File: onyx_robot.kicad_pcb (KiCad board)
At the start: 2 copper layers, 50 x 50 mm, 32 parts, among them P1 EXT1, P2 EXT2, P3 READER, P4 FTDI, Q1 Q_NMOS_GSD, Q2 Q_NMOS_GSD, SW1 RESET, U1 ADP2301, U2 RELAY_SPDT, U3 ESP-12E

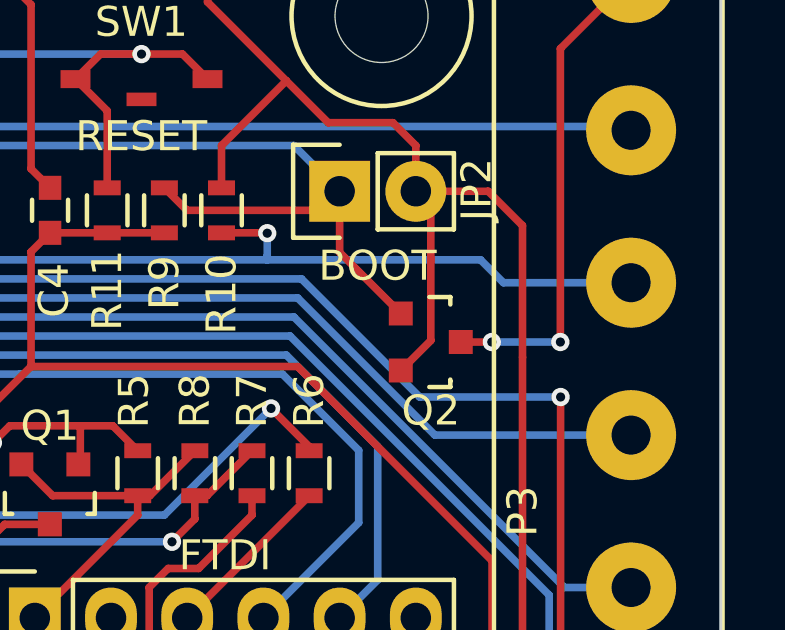
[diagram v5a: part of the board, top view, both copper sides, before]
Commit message: Increased clearance between Q2 and screw terminals
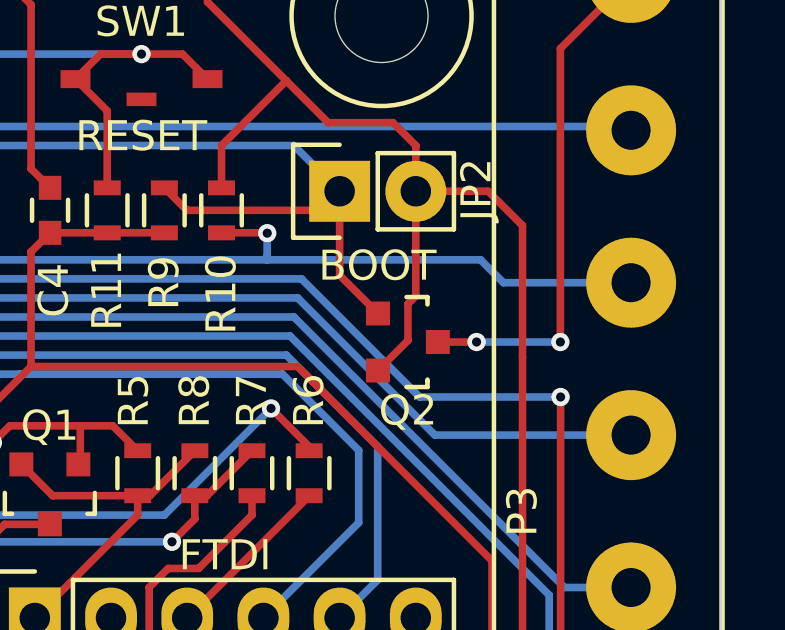
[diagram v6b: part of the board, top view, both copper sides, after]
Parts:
- moved Q2 0.76 mm to (84.6, 54.7)
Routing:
- net PIEZO: track 16.4 -> 17.2 mm
- net GND: track 274.5 -> 275.1 mm
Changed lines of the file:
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@@
     (links 76)
     (no_connects 0)
-    (area 44.949999 39.949999 95.050001 90.050001)
+    (area 44.679799 39.675999 95.388501 91.2244)
     (thickness 1.6)
     (drawings 26)
-    (tracks 367)
+    (tracks 369)
     (zones 0)
     (modules 32)
@@
   )
   (module Housings_SOT-23_SOT-143_TSOT-6:SOT-23 (layer F.Cu)
-    (at 85.336 54.682 270)
+    (at 84.574 54.682 270)
     (descr "SOT-23, Standard")
     (tags SOT-23)
@@
   (segment (start 81.15795 79.78775) (end 80.49755 80.44815) (width 0.254) (layer F.Cu) (net 1))
   (segment (start 80.49755 80.44815) (end 79.62843 80.44815) (width 0.254) (layer F.Cu) (net 1))
-  (segment (start 84.836 49.657) (end 85.336 50.157) (width 0.254) (layer F.Cu) (net 2) (status C00000))
-  (segment (start 85.336 50.157) (end 85.336 54.63124) (width 0.254) (layer F.Cu) (net 2) (status 400000))
-  (segment (start 85.336 54.63124) (end 84.33524 55.632) (width 0.254) (layer F.Cu) (net 2) (status 800000))
-  (segment (start 72.136 63.881) (end 75.565 60.452) (width 0.254) (layer F.Cu) (net 2) (status 400000))
-  (segment (start 75.565 60.452) (end 75.565 59.805) (width 0.254) (layer F.Cu) (net 2) (status 800000))
-  (segment (start 71.686 58.76124) (end 72.72976 59.805) (width 0.254) (layer F.Cu) (net 2) (status 400000))
-  (segment (start 72.72976 59.805) (end 75.565 59.805) (width 0.254) (layer F.Cu) (net 2) (status 800000))
+  (segment (start 84.836 49.657) (end 84.836 53.15) (width 0.254) (layer F.Cu) (net 2) (status 400000))
+  (segment (start 84.574 54.63124) (end 83.57324 55.632) (width 0.254) (layer F.Cu) (net 2) (status 800000))
+  (segment (start 84.574 53.412) (end 84.574 54.63124) (width 0.254) (layer F.Cu) (net 2))
+  (segment (start 84.836 53.15) (end 84.574 53.412) (width 0.254) (layer F.Cu) (net 2))
+  (segment (start 84.836 49.657) (end 85.336 50.157) (width 0.254) (layer F.Cu) (net 2))
+  (segment (start 72.136 63.881) (end 75.565 60.452) (width 0.254) (layer F.Cu) (net 2))
+  (segment (start 75.565 60.452) (end 75.565 59.805) (width 0.254) (layer F.Cu) (net 2))
+  (segment (start 71.686 58.76124) (end 72.72976 59.805) (width 0.254) (layer F.Cu) (net 2))
+  (segment (start 72.72976 59.805) (end 75.565 59.805) (width 0.254) (layer F.Cu) (net 2))
   (segment (start 84.63153 76.46035) (end 85.217 77.04582) (width 0.254) (layer F.Cu) (net 2))
   (segment (start 85.217 77.04582) (end 85.217 78.867) (width 0.254) (layer F.Cu) (net 2))
@@
   (segment (start 77.61115 77.05467) (end 77.28835 76.73187) (width 0.254) (layer F.Cu) (net 5))
   (segment (start 77.28835 76.73187) (end 77.28835 75.23215) (width 0.254) (layer F.Cu) (net 5))
-  (segment (start 72.636 60.76022) (end 71.12978 60.76022) (width 0.254) (layer F.Cu) (net 6) (status 400000))
-  (segment (start 70.096 66.82702) (end 71.628 68.35902) (width 0.254) (layer F.Cu) (net 6) (status 800000))
+  (segment (start 72.636 60.76022) (end 71.12978 60.76022) (width 0.254) (layer F.Cu) (net 6))
+  (segment (start 70.096 66.82702) (end 71.628 68.35902) (width 0.254) (layer F.Cu) (net 6))
   (segment (start 70.096 61.794) (end 70.096 66.82702) (width 0.254) (layer F.Cu) (net 6))
   (segment (start 71.12978 60.76022) (end 70.096 61.794) (width 0.254) (layer F.Cu) (net 6))
@@
   (segment (start 58.166 80.518) (end 60.198 82.55) (width 0.8) (layer B.Cu) (net 9))
   (segment (start 58.166 67.746) (end 58.166 80.518) (width 0.8) (layer B.Cu) (net 9))
-  (segment (start 82.296 49.657) (end 82.296 51.69276) (width 0.254) (layer F.Cu) (net 10) (status 400000))
-  (segment (start 82.296 51.69276) (end 84.33524 53.732) (width 0.254) (layer F.Cu) (net 10) (status 800000))
+  (segment (start 82.296 49.657) (end 82.296 52.45476) (width 0.254) (layer F.Cu) (net 10) (status 400000))
+  (segment (start 82.296 52.45476) (end 83.57324 53.732) (width 0.254) (layer F.Cu) (net 10) (status 800000))
   (segment (start 82.296 49.657) (end 81.661 50.292) (width 0.254) (layer F.Cu) (net 10))
   (segment (start 81.661 50.292) (end 77.204 50.292) (width 0.254) (layer F.Cu) (net 10))
@@
   (via (at 58.039 45.339) (size 0.6096) (drill 0.3048) (layers F.Cu B.Cu) (net 19))
   (segment (start 60.198 47.498) (end 58.039 45.339) (width 0.254) (layer B.Cu) (net 19))
-  (segment (start 92.0115 42.545) (end 89.654 44.9025) (width 0.254) (layer F.Cu) (net 20) (status 400000))
-  (segment (start 87.368 54.682) (end 86.33422 54.682) (width 0.254) (layer F.Cu) (net 20) (status 800000))
-  (via (at 87.368 54.682) (size 0.6096) (drill 0.3048) (layers F.Cu B.Cu) (net 20))
-  (segment (start 89.654 54.682) (end 87.368 54.682) (width 0.254) (layer B.Cu) (net 20))
+  (segment (start 92.0115 42.545) (end 89.654 44.9025) (width 0.254) (layer F.Cu) (net 20))
+  (segment (start 89.654 44.9025) (end 89.654 54.682) (width 0.254) (layer F.Cu) (net 20))
   (via (at 89.654 54.682) (size 0.6096) (drill 0.3048) (layers F.Cu B.Cu) (net 20))
-  (segment (start 89.654 44.9025) (end 89.654 54.682) (width 0.254) (layer F.Cu) (net 20))
+  (segment (start 89.654 54.682) (end 86.86 54.682) (width 0.254) (layer B.Cu) (net 20))
+  (via (at 86.86 54.682) (size 0.6096) (drill 0.3048) (layers F.Cu B.Cu) (net 20))
+  (segment (start 86.86 54.682) (end 85.57222 54.682) (width 0.254) (layer F.Cu) (net 20) (status 800000))
   (segment (start 82.931 58.293) (end 82.931 60.706) (width 0.254) (layer B.Cu) (net 21))
   (segment (start 80.391 55.753) (end 82.931 58.293) (width 0.254) (layer B.Cu) (net 21))
@@
   (segment (start 80.518 55.118) (end 83.566 58.166) (width 0.254) (layer B.Cu) (net 22))
   (segment (start 83.566 62.611) (end 82.296 63.881) (width 0.254) (layer B.Cu) (net 22))
-  (segment (start 73.586 58.76124) (end 73.652 58.69524) (width 0.254) (layer F.Cu) (net 23) (status C00000))
-  (segment (start 73.652 58.69524) (end 73.652 57.476) (width 0.254) (layer F.Cu) (net 23) (status 400000))
+  (segment (start 73.586 58.76124) (end 73.652 58.69524) (width 0.254) (layer F.Cu) (net 23))
+  (segment (start 73.652 58.69524) (end 73.652 57.476) (width 0.254) (layer F.Cu) (net 23))
   (segment (start 70.739 58.039) (end 71.302 57.476) (width 0.254) (layer F.Cu) (net 23))
-  (segment (start 74.736 57.476) (end 75.565 58.305) (width 0.254) (layer F.Cu) (net 23) (status 800000))
+  (segment (start 74.736 57.476) (end 75.565 58.305) (width 0.254) (layer F.Cu) (net 23))
   (segment (start 71.302 57.476) (end 73.652 57.476) (width 0.254) (layer F.Cu) (net 23))
   (segment (start 73.652 57.476) (end 74.736 57.476) (width 0.254) (layer F.Cu) (net 23))

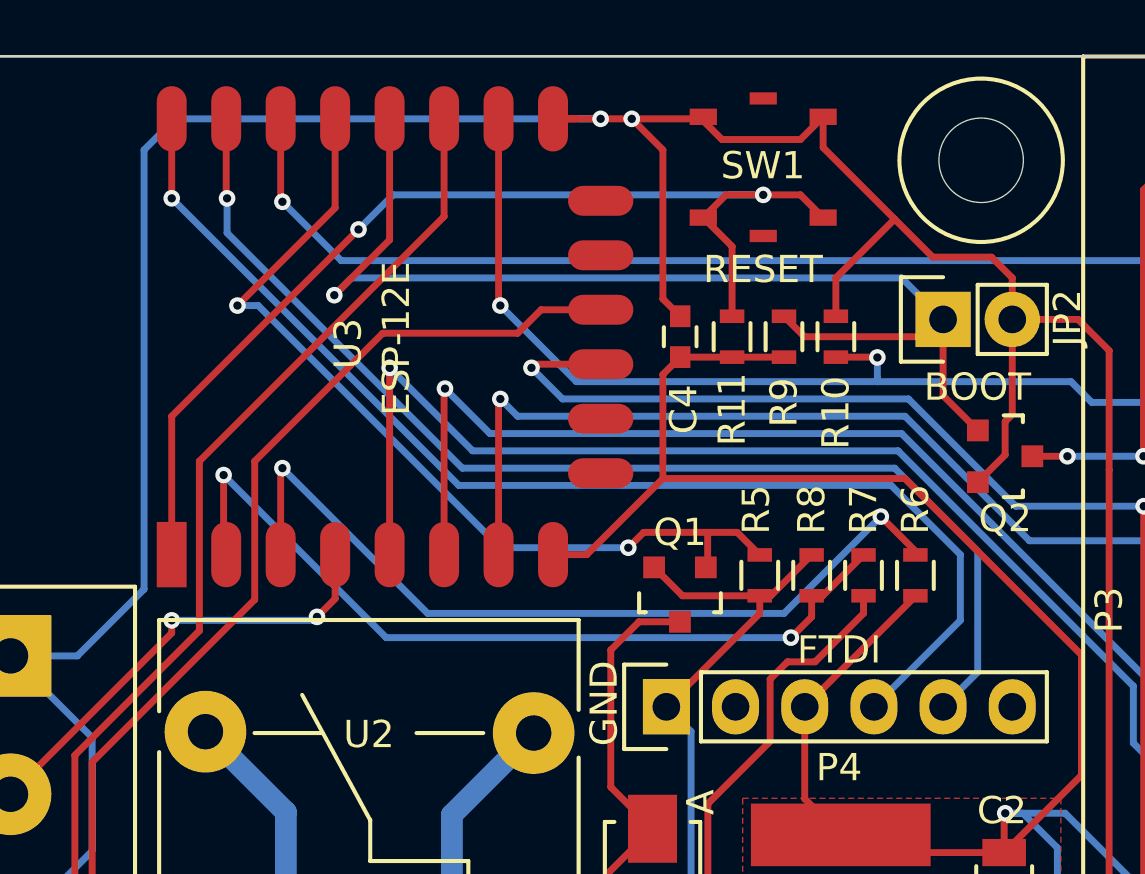
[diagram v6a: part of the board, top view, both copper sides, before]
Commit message: Fix RX/TX in PCB and regenerate all files
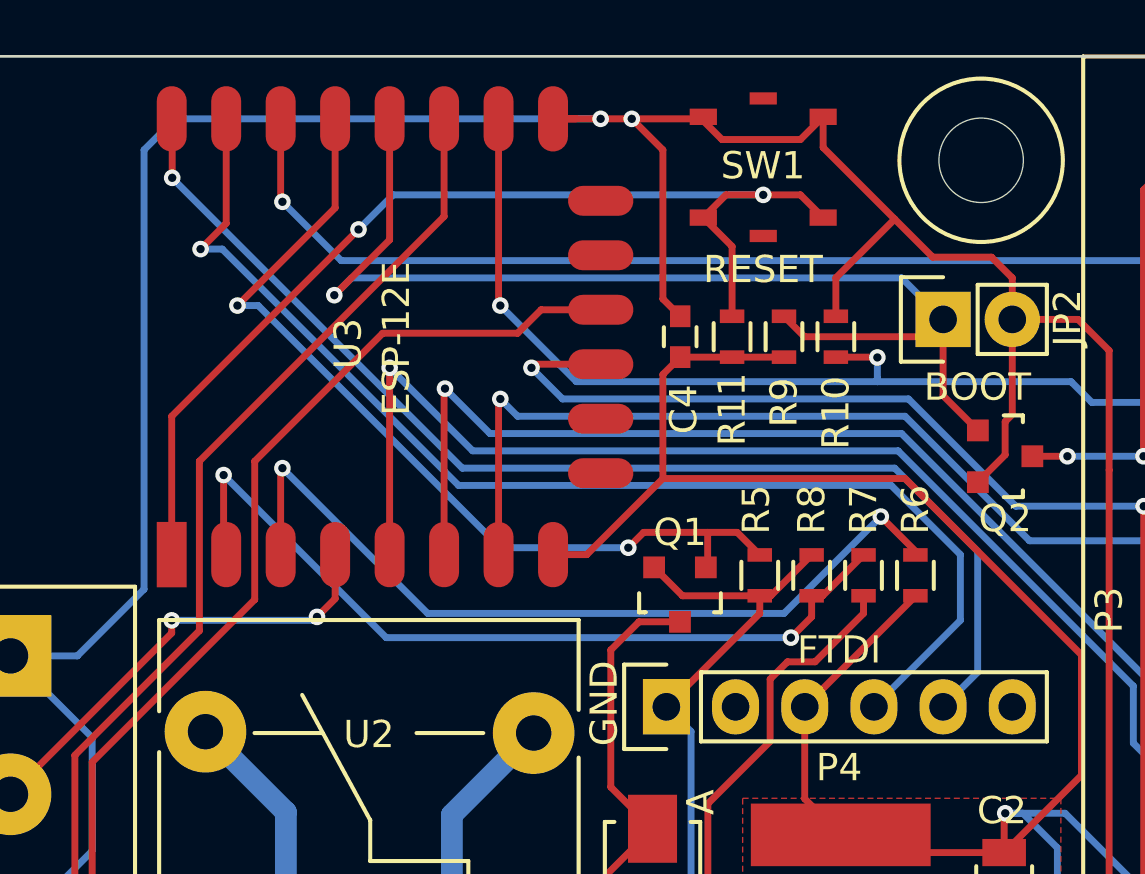
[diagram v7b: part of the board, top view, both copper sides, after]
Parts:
- R2: value 20K2 1% -> 10K2 1%
- R7: value 10K 1% -> 31K6 1%
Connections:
- P4 pad 4: TX -> RX
- P4 pad 5: RX -> TX
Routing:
- net RX: track 42.8 -> 44.6 mm
- net TX: track 44.2 -> 43.7 mm
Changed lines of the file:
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@@
     (thickness 1.6)
     (drawings 26)
-    (tracks 369)
+    (tracks 372)
     (zones 0)
     (modules 32)
@@
       (net 3 +3V3))
     (pad 4 thru_hole oval (at 0 7.62 90) (size 2.032 1.7272) (drill 1.016) (layers *.Cu *.Mask F.SilkS)
+      (net 22 RX))
+    (pad 5 thru_hole oval (at 0 10.16 90) (size 2.032 1.7272) (drill 1.016) (layers *.Cu *.Mask F.SilkS)
       (net 21 TX))
-    (pad 5 thru_hole oval (at 0 10.16 90) (size 2.032 1.7272) (drill 1.016) (layers *.Cu *.Mask F.SilkS)
-      (net 22 RX))
     (pad 6 thru_hole oval (at 0 12.7 90) (size 2.032 1.7272) (drill 1.016) (layers *.Cu *.Mask F.SilkS))
     (model Pin_Headers.3dshapes/Pin_Header_Straight_1x06.wrl
@@
       (effects (font (size 1 1) (thickness 0.15)))
     )
-    (fp_text value "20K2 1%" (at 0 1.9 90) (layer F.Fab)
+    (fp_text value "10K2 1%" (at 0 1.9 90) (layer F.Fab)
       (effects (font (size 1 1) (thickness 0.15)))
     )
@@
       (effects (font (size 1 1) (thickness 0.15)))
     )
-    (fp_text value "10K 1%" (at 0 1.9 90) (layer F.Fab)
+    (fp_text value "31K6 1%" (at 0 1.9 90) (layer F.Fab)
       (effects (font (size 1 1) (thickness 0.15)))
     )
@@
   (segment (start 81.15795 79.78775) (end 80.49755 80.44815) (width 0.254) (layer F.Cu) (net 1))
   (segment (start 80.49755 80.44815) (end 79.62843 80.44815) (width 0.254) (layer F.Cu) (net 1))
-  (segment (start 84.836 49.657) (end 84.836 53.15) (width 0.254) (layer F.Cu) (net 2) (status 400000))
-  (segment (start 84.574 54.63124) (end 83.57324 55.632) (width 0.254) (layer F.Cu) (net 2) (status 800000))
+  (segment (start 84.836 49.657) (end 84.836 53.15) (width 0.254) (layer F.Cu) (net 2))
+  (segment (start 84.574 54.63124) (end 83.57324 55.632) (width 0.254) (layer F.Cu) (net 2))
   (segment (start 84.574 53.412) (end 84.574 54.63124) (width 0.254) (layer F.Cu) (net 2))
   (segment (start 84.836 53.15) (end 84.574 53.412) (width 0.254) (layer F.Cu) (net 2))
@@
   (segment (start 58.166 80.518) (end 60.198 82.55) (width 0.8) (layer B.Cu) (net 9))
   (segment (start 58.166 67.746) (end 58.166 80.518) (width 0.8) (layer B.Cu) (net 9))
-  (segment (start 82.296 49.657) (end 82.296 52.45476) (width 0.254) (layer F.Cu) (net 10) (status 400000))
-  (segment (start 82.296 52.45476) (end 83.57324 53.732) (width 0.254) (layer F.Cu) (net 10) (status 800000))
+  (segment (start 82.296 49.657) (end 82.296 52.45476) (width 0.254) (layer F.Cu) (net 10))
+  (segment (start 82.296 52.45476) (end 83.57324 53.732) (width 0.254) (layer F.Cu) (net 10))
   (segment (start 82.296 49.657) (end 81.661 50.292) (width 0.254) (layer F.Cu) (net 10))
   (segment (start 81.661 50.292) (end 77.204 50.292) (width 0.254) (layer F.Cu) (net 10))
@@
   (segment (start 89.654 54.682) (end 86.86 54.682) (width 0.254) (layer B.Cu) (net 20))
   (via (at 86.86 54.682) (size 0.6096) (drill 0.3048) (layers F.Cu B.Cu) (net 20))
-  (segment (start 86.86 54.682) (end 85.57222 54.682) (width 0.254) (layer F.Cu) (net 20) (status 800000))
-  (segment (start 82.931 58.293) (end 82.931 60.706) (width 0.254) (layer B.Cu) (net 21))
-  (segment (start 80.391 55.753) (end 82.931 58.293) (width 0.254) (layer B.Cu) (net 21))
-  (segment (start 53.975 42.293) (end 53.975 45.212) (width 0.254) (layer F.Cu) (net 21) (status 10))
-  (via (at 53.975 45.212) (size 0.6096) (drill 0.3048) (layers F.Cu B.Cu) (net 21))
-  (segment (start 64.516 55.753) (end 53.975 45.212) (width 0.254) (layer B.Cu) (net 21))
-  (segment (start 71.628 55.753) (end 64.516 55.753) (width 0.254) (layer B.Cu) (net 21))
-  (segment (start 71.628 55.753) (end 80.391 55.753) (width 0.254) (layer B.Cu) (net 21))
-  (segment (start 82.931 60.706) (end 79.756 63.881) (width 0.254) (layer B.Cu) (net 21))
-  (segment (start 83.566 58.166) (end 83.566 62.611) (width 0.254) (layer B.Cu) (net 22))
-  (segment (start 55.975 42.293) (end 55.975 45.18) (width 0.254) (layer F.Cu) (net 22) (status 10))
-  (segment (start 56.007 45.212) (end 55.975 45.18) (width 0.254) (layer F.Cu) (net 22))
-  (via (at 56.007 45.212) (size 0.6096) (drill 0.3048) (layers F.Cu B.Cu) (net 22))
-  (segment (start 56.007 46.482) (end 56.007 45.212) (width 0.254) (layer B.Cu) (net 22))
-  (segment (start 64.643 55.118) (end 56.007 46.482) (width 0.254) (layer B.Cu) (net 22))
-  (segment (start 80.518 55.118) (end 64.643 55.118) (width 0.254) (layer B.Cu) (net 22))
-  (segment (start 80.518 55.118) (end 83.566 58.166) (width 0.254) (layer B.Cu) (net 22))
-  (segment (start 83.566 62.611) (end 82.296 63.881) (width 0.254) (layer B.Cu) (net 22))
+  (segment (start 86.86 54.682) (end 85.57222 54.682) (width 0.254) (layer F.Cu) (net 20))
+  (segment (start 53.9924 42.3104) (end 53.975 42.293) (width 0.254) (layer F.Cu) (net 21))
+  (segment (start 53.9924 44.4585) (end 53.9924 42.3104) (width 0.254) (layer F.Cu) (net 21))
+  (via (at 53.9924 44.4585) (size 0.6096) (drill 0.3048) (layers F.Cu B.Cu) (net 21))
+  (segment (start 53.9924 44.4674) (end 53.9924 44.4585) (width 0.254) (layer B.Cu) (net 21))
+  (segment (start 64.643 55.118) (end 53.9924 44.4674) (width 0.254) (layer B.Cu) (net 21))
+  (segment (start 80.518 55.118) (end 64.643 55.118) (width 0.254) (layer B.Cu) (net 21))
+  (segment (start 82.296 63.881) (end 83.566 62.611) (width 0.254) (layer B.Cu) (net 21))
+  (segment (start 80.518 55.118) (end 83.566 58.166) (width 0.254) (layer B.Cu) (net 21))
+  (segment (start 83.566 58.166) (end 83.566 62.611) (width 0.254) (layer B.Cu) (net 21))
+  (segment (start 64.508 55.753) (end 55.8297 47.0747) (width 0.254) (layer B.Cu) (net 22))
+  (segment (start 55.975 46.1335) (end 55.975 42.293) (width 0.254) (layer F.Cu) (net 22))
+  (segment (start 55.0338 47.0747) (end 55.975 46.1335) (width 0.254) (layer F.Cu) (net 22))
+  (via (at 55.0338 47.0747) (size 0.6096) (drill 0.3048) (layers F.Cu B.Cu) (net 22))
+  (segment (start 55.8297 47.0747) (end 55.0338 47.0747) (width 0.254) (layer B.Cu) (net 22))
+  (segment (start 71.628 55.753) (end 64.508 55.753) (width 0.254) (layer B.Cu) (net 22))
+  (segment (start 64.508 55.753) (end 64.516 55.753) (width 0.254) (layer B.Cu) (net 22))
+  (segment (start 71.628 55.753) (end 80.391 55.753) (width 0.254) (layer B.Cu) (net 22))
+  (segment (start 80.391 55.753) (end 82.931 58.293) (width 0.254) (layer B.Cu) (net 22))
+  (segment (start 82.931 60.706) (end 79.756 63.881) (width 0.254) (layer B.Cu) (net 22))
+  (segment (start 82.931 58.293) (end 82.931 60.706) (width 0.254) (layer B.Cu) (net 22))
   (segment (start 73.586 58.76124) (end 73.652 58.69524) (width 0.254) (layer F.Cu) (net 23))
   (segment (start 73.652 58.69524) (end 73.652 57.476) (width 0.254) (layer F.Cu) (net 23))

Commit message: Version 2
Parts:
- removed the REF** at (56.4, 86.1)
- removed the REF** at (83.7, 43.8)
- added R12: 2K2, Resistors_SMD:R_0603, F.Cu at (85.2, 59.1)
- added R13: 2K2, Resistors_SMD:R_0603, F.Cu at (83.3, 59.1)
- added R14: 10K, Resistors_SMD:R_0603, F.Cu at (78.4, 50.3)
- added REF**: MountingHole M3+, timhawes:MountingHole_M3+, F.Cu at (56.7, 85.9)
- added REF**: MountingHole M3+, timhawes:MountingHole_M3+, F.Cu at (90.9, 85.9)
- added REF**: MountingHole M3+, timhawes:MountingHole_M3+, F.Cu at (83.3, 44.1)
- P1: value EXT1 -> POWER; footprint timhawes:Terminal_Block_5.08mm_x6 -> timhawes:Terminal_Block_5.08mm_x4
- P2: value EXT2 -> INPUTS
- R5: value 10K -> 100R
- moved R10 9.20 mm to (75.5, 59.1)
- moved R5 6.34 mm to (77.4, 53.0), turned to 0 degrees
- moved P1 3.16 mm to (76.5, 87.0)
- moved JP1 1.65 mm to (64.0, 83.0)
- moved Q2 1.40 mm to (85.3, 53.5)
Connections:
- net MISO renamed SCL
- P1 pad 1: GND -> 12V_OUT
- P1 pad 2: 12V_OUT -> GND
- P1 pad 3: GND -> +12V
- P1 pad 4: +12V -> GND
- P2 pad 4: DOOR_SENSE -> DOOR
- P2 pad 6: TAMPER -> SNIB
- P3 pad 3: CLK -> SDA
- P3 pad 5: MOSI -> PN532_RESET
- P3 pad 6: CS -> Net-(P3-Pad6)
- P3 pad 7: LED -> PIEZO
- P3 pad 8: PIEZO -> (no net)
- R10 pad 1: CS -> RELAY
- R5 pad 1: RELAY -> LED
- R5 pad 2: GND -> Net-(P3-Pad6)
- U3 pad 11: SNIB -> (no net)
- U3 pad 12: TAMPER -> (no net)
- U3 pad 16: CS -> RELAY
- U3 pad 17: DOOR_SENSE -> PN532_RESET
- U3 pad 19: RELAY -> EXIT
- U3 pad 20: LED -> SNIB
- U3 pad 4: EXIT -> LED
- U3 pad 5: CLK -> DOOR
- U3 pad 7: MOSI -> SDA
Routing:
- net TAMPER: track 51.3 -> 0.00 mm
- net SDA: track 0.00 -> 45.7 mm, vias 0 -> 2
- net CLK: track 45.0 -> 0.00 mm, vias 1 -> 0
- net DOOR_SENSE: track 41.6 -> 0.00 mm
- net PN532_RESET: track 0.00 -> 38.5 mm, vias 0 -> 1
- net CS: track 37.2 -> 0.00 mm, vias 2 -> 0
- net MOSI: track 33.9 -> 0.00 mm, vias 1 -> 0
- net DOOR: track 0.00 -> 30.8 mm
- net Net-(P3-Pad6): track 0.00 -> 17.4 mm, vias 0 -> 1
- net EXIT: track 17.4 -> 33.1 mm
- net LED: track 38.2 -> 23.9 mm, vias 1 -> 2
- net SCL: track 38.6 -> 47.0 mm, vias 1 -> 2
- net RELAY: track 33.2 -> 25.6 mm
- net +3V3: track 97.9 -> 92.0 mm
- net 12V_OUT: track 11.4 -> 5.52 mm
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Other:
- board text added: "DOOR"
- board text added: "RESET"
- board text added: "SCL"
- board text added: "SDA"
- board text added: "timhawes.com/or2 edinburghhacklab.com"
- board text removed: "CLK"
- board text removed: "CS"
- board text removed: "DOOR_SENSE"
- board text removed: "MISO"
- board text removed: "MOSI"
- board text removed: "TAMPER"
- board text removed: "timhawes.com/or1 edinburghhacklab.com"
